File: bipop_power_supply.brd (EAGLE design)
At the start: 160 x 100 mm, 20 parts, among them IC1 LM1117MP-3.3, IC2 LM1117MP-5.0

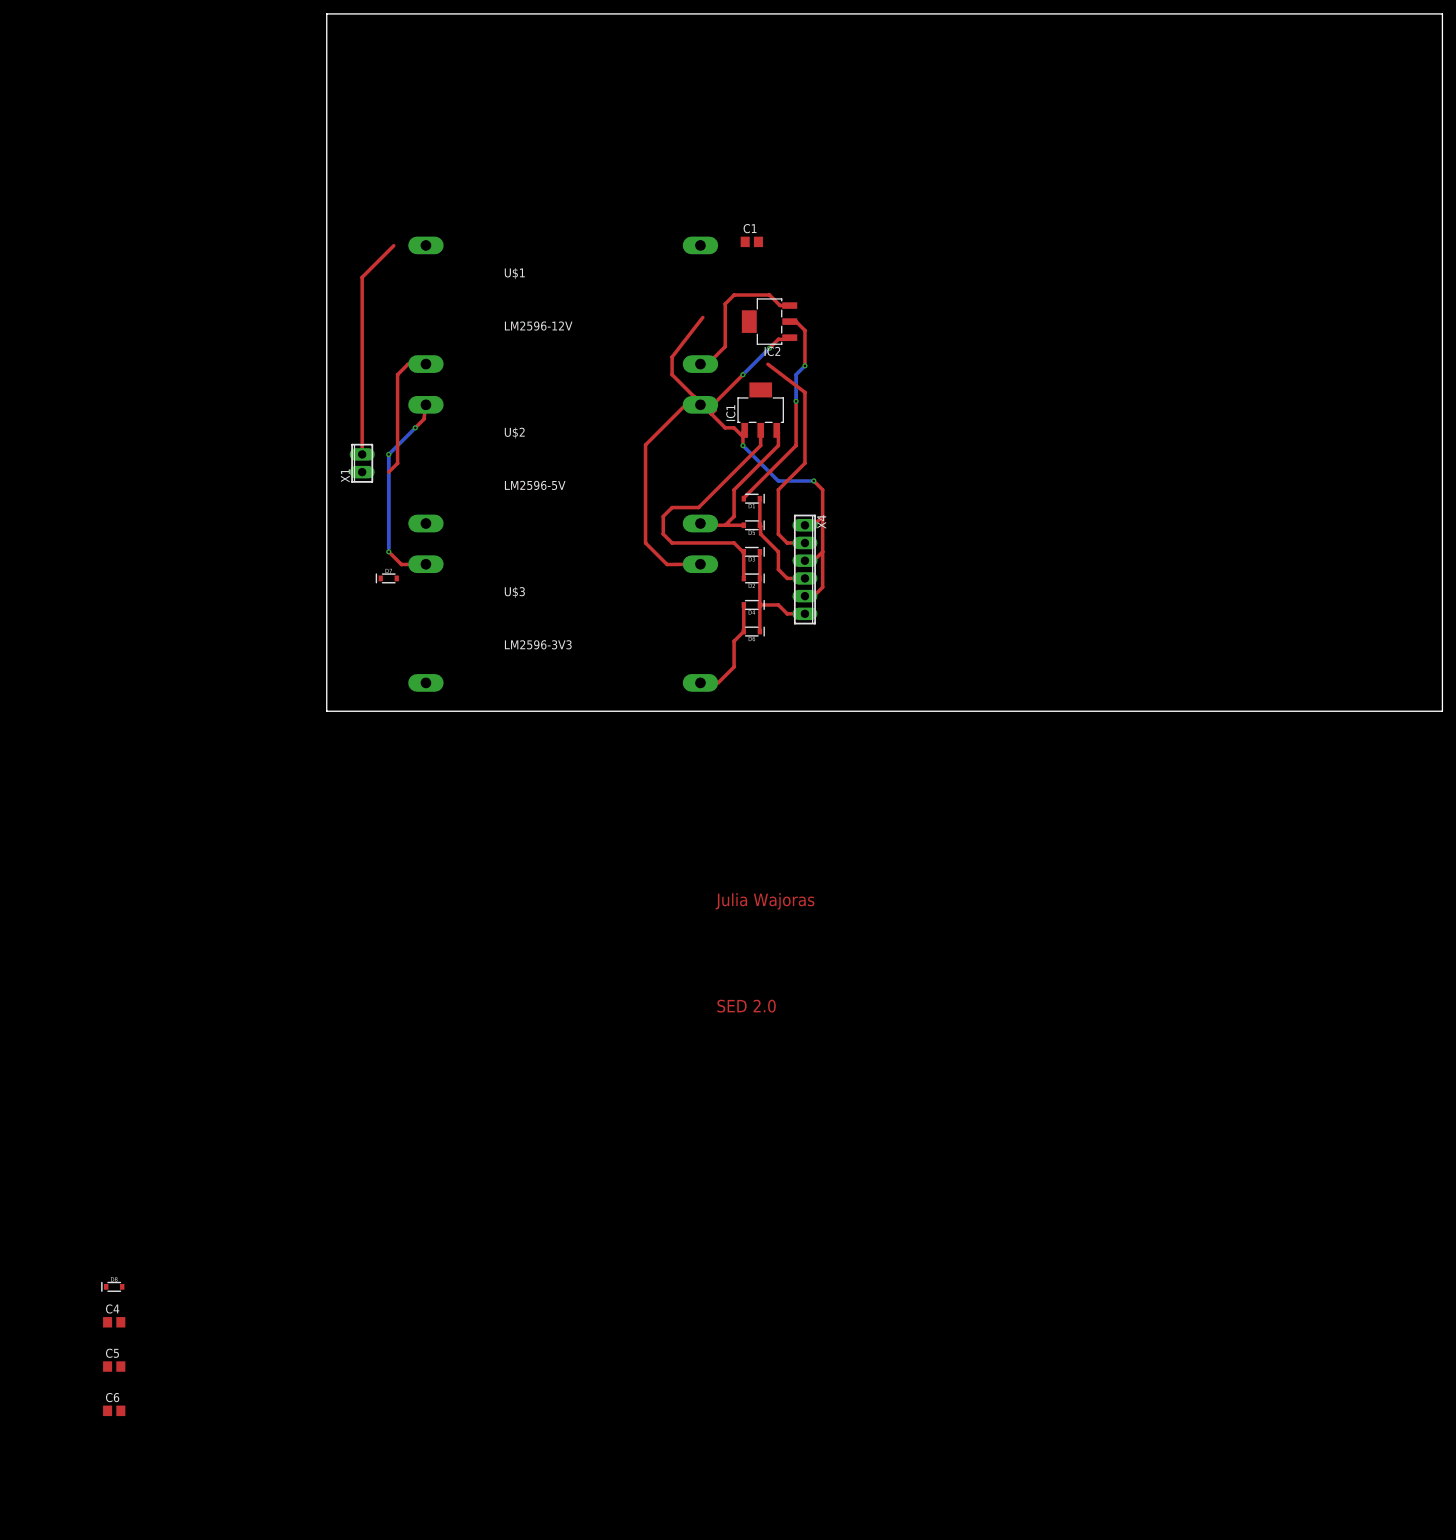
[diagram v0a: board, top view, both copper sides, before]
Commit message: .sch z diodami i kondensatorami, .brd TODO
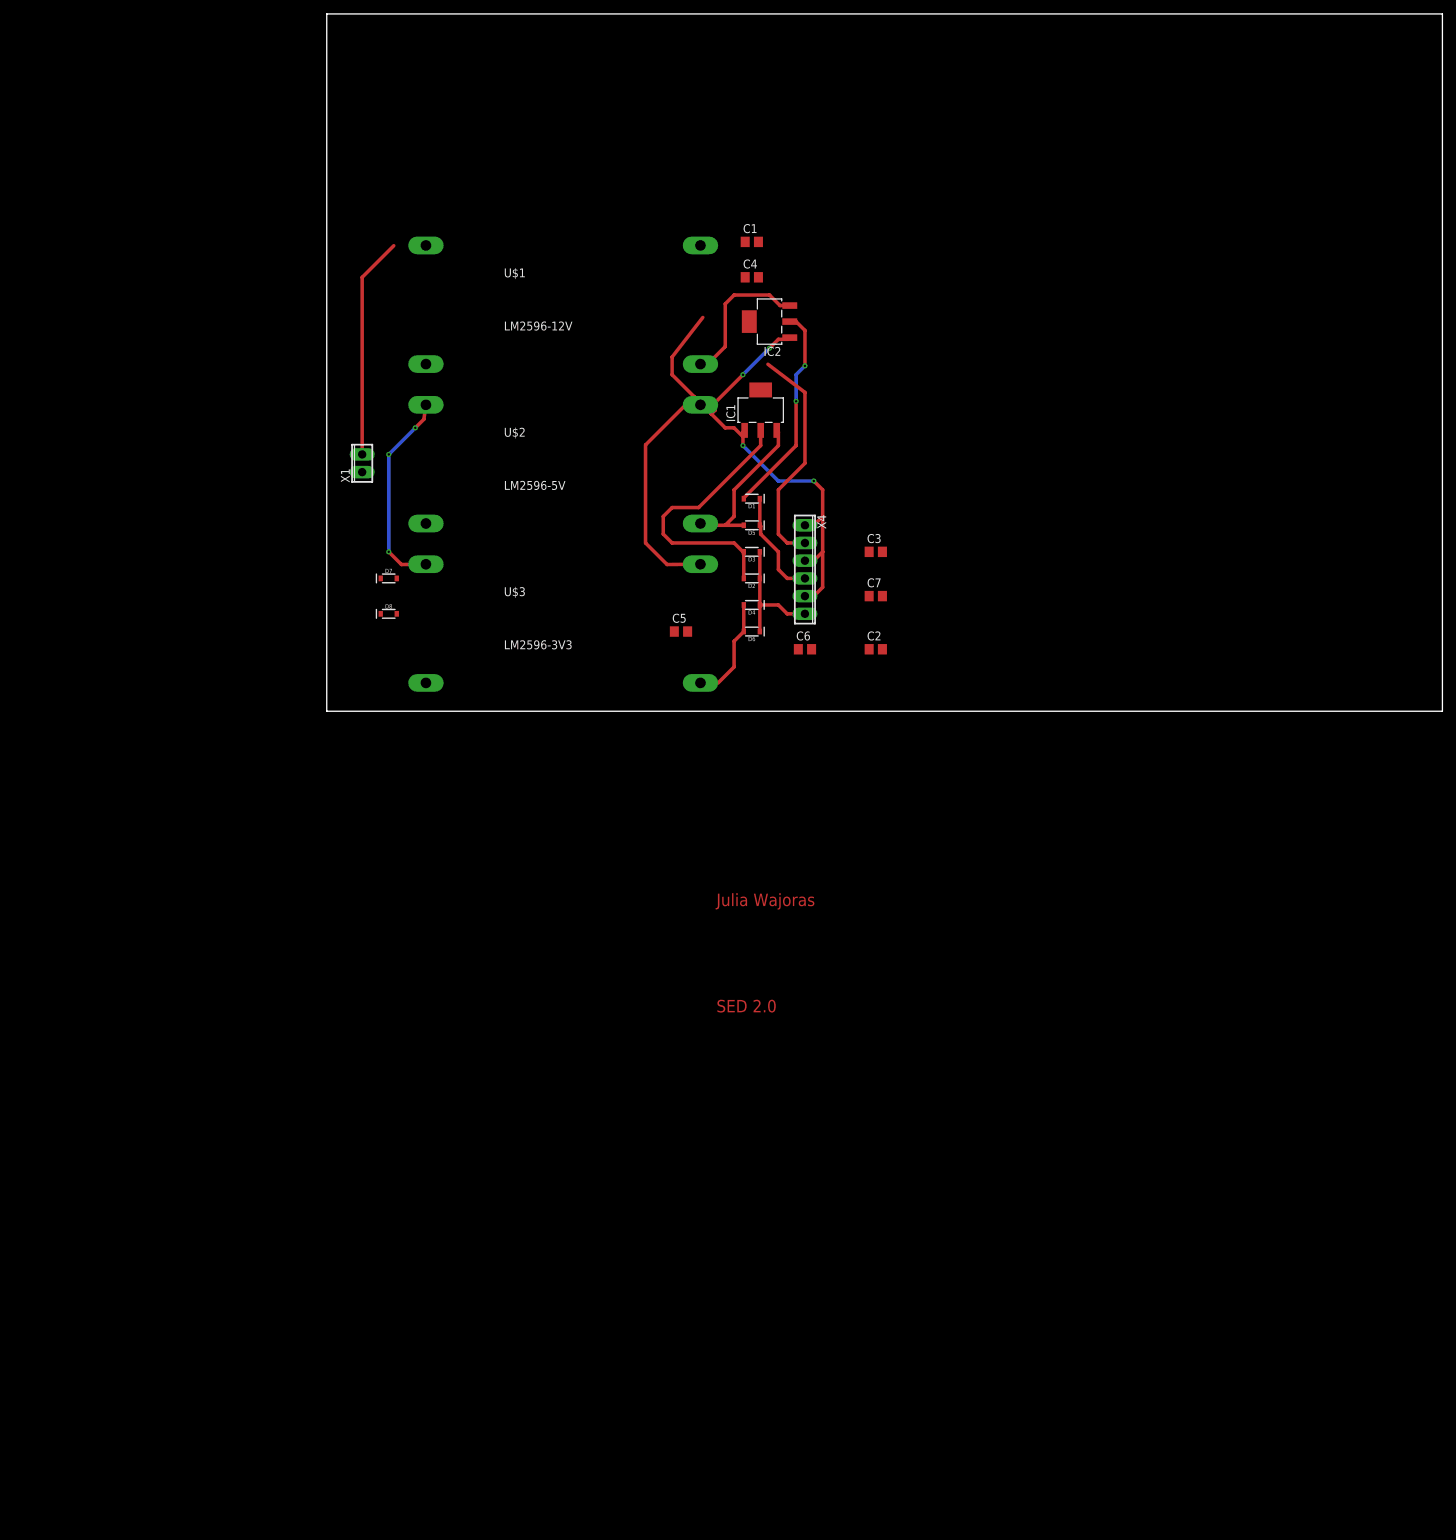
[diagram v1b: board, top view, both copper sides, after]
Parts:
- added C2, C3, C7: 100uF, rcl:C0805
- moved C4 175.6 mm to (61.0, 62.2)
- moved C6 147.5 mm to (68.6, 8.89)
- moved C5 133.1 mm to (50.8, 11.4)
- moved D8 104.2 mm to (8.89, 14.0)
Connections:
- removed net N$2: C1.2, C4.2, IC2.3, U$1.V_OUT+, X4.2
- removed net N$6: C1.1, C4.1, U$1.V_OUT-
- new net C12+: C7.1, IC2.3, U$1.V_OUT+, X4.2
- new net N$10: C1.1, C4.2
- new net N$12: C1.2, C3.1
- new net N$8: C2.2, C5.1
- new net N$9: C4.1, C7.2
- net GND: now also C2.1, C3.2, U$1.V_OUT-; no longer C5.1
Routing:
- net N$2: track 53.0 -> 0.00 mm
- net C12+: track 0.00 -> 53.0 mm
- net N$22: track 20.9 -> 1.75 mm
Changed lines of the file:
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@@
 </element>
 <element name="C1" library="rcl" library_urn="urn:adsk.eagle:library:334" package="C0805" package3d_urn="urn:adsk.eagle:package:23617/2" value="100uF" x="60.96" y="67.31"/>
-<element name="D8" library="SparkFun-DiscreteSemi" package="SOD-323" value="33.3V" x="-30.48" y="-82.55">
-<attribute name="PROD_ID" value="DIO-11284" x="-30.48" y="-82.55" size="1.778" layer="27" display="off"/>
+<element name="D8" library="SparkFun-DiscreteSemi" package="SOD-323" value="33.3V" x="8.89" y="13.97">
+<attribute name="PROD_ID" value="DIO-11284" x="8.89" y="13.97" size="1.778" layer="27" display="off"/>
 </element>
-<element name="C4" library="rcl" library_urn="urn:adsk.eagle:library:334" package="C0805" package3d_urn="urn:adsk.eagle:package:23617/2" value="100uF" x="-30.48" y="-87.63"/>
-<element name="C5" library="rcl" library_urn="urn:adsk.eagle:library:334" package="C0805" package3d_urn="urn:adsk.eagle:package:23617/2" value="100uF" x="-30.48" y="-93.98"/>
-<element name="C6" library="rcl" library_urn="urn:adsk.eagle:library:334" package="C0805" package3d_urn="urn:adsk.eagle:package:23617/2" value="100uF" x="-30.48" y="-100.33"/>
+<element name="C4" library="rcl" library_urn="urn:adsk.eagle:library:334" package="C0805" package3d_urn="urn:adsk.eagle:package:23617/2" value="100uF" x="60.96" y="62.23"/>
+<element name="C5" library="rcl" library_urn="urn:adsk.eagle:library:334" package="C0805" package3d_urn="urn:adsk.eagle:package:23617/2" value="100uF" x="50.8" y="11.43"/>
+<element name="C6" library="rcl" library_urn="urn:adsk.eagle:library:334" package="C0805" package3d_urn="urn:adsk.eagle:package:23617/2" value="100uF" x="68.58" y="8.89"/>
+<element name="C2" library="rcl" library_urn="urn:adsk.eagle:library:334" package="C0805" package3d_urn="urn:adsk.eagle:package:23617/2" value="100uF" x="78.74" y="8.89"/>
+<element name="C3" library="rcl" library_urn="urn:adsk.eagle:library:334" package="C0805" package3d_urn="urn:adsk.eagle:package:23617/2" value="100uF" x="78.74" y="22.86"/>
+<element name="C7" library="rcl" library_urn="urn:adsk.eagle:library:334" package="C0805" package3d_urn="urn:adsk.eagle:package:23617/2" value="100uF" x="78.74" y="16.51"/>
 </elements>
 <signals>
@@
 <wire x1="66.16" y1="53.34" x2="66.4" y2="53.58" width="0.508" layer="1"/>
 <contactref element="C6" pad="1"/>
-<contactref element="C5" pad="1"/>
+<contactref element="C2" pad="1"/>
 <contactref element="U$2" pad="V_OUT-"/>
-<wire x1="-31.43" y1="-93.98" x2="-31.43" y2="-100.33" width="0" layer="19" extent="1-1"/>
-<wire x1="48.81" y1="21.04" x2="-31.43" y2="-93.98" width="0" layer="19" extent="1-1"/>
+<contactref element="U$1" pad="V_OUT-"/>
+<contactref element="C3" pad="2"/>
+<wire x1="77.79" y1="8.89" x2="79.69" y2="22.86" width="0" layer="19" extent="1-1"/>
+<wire x1="67.63" y1="8.89" x2="77.79" y2="8.89" width="0" layer="19" extent="1-1"/>
+<wire x1="48.81" y1="21.04" x2="67.63" y2="8.89" width="0" layer="19" extent="1-1"/>
 <wire x1="53.93" y1="43.86" x2="53.89" y2="43.9" width="0" layer="19" extent="1-1"/>
 <wire x1="53.594" y1="43.942" x2="53.89" y2="43.9" width="0" layer="19" extent="1-1"/>
+<wire x1="53.594" y1="66.802" x2="53.93" y2="56.47" width="0" layer="19" extent="1-1"/>
 </signal>
 <signal name="N$5">
@@
 <contactref element="C6" pad="2"/>
 <contactref element="U$3" pad="V_OUT+"/>
-<wire x1="53.594" y1="4.064" x2="-29.53" y2="-100.33" width="0" layer="19" extent="1-1"/>
+<wire x1="53.594" y1="4.064" x2="69.53" y2="8.89" width="0" layer="19" extent="1-1"/>
 <wire x1="56.11" y1="4.04" x2="53.594" y2="4.064" width="0" layer="19" extent="1-1"/>
 </signal>
@@
 <wire x1="58.42" y1="31.75" x2="58.42" y2="27.94" width="0.508" layer="1"/>
 <contactref element="C5" pad="2"/>
-<wire x1="53.594" y1="26.924" x2="-29.53" y2="-93.98" width="0" layer="19" extent="1-1"/>
+<wire x1="53.594" y1="26.924" x2="51.75" y2="11.43" width="0" layer="19" extent="1-1"/>
 </signal>
 <signal name="N$11">
@@
 <wire x1="8.89" y1="36.83" x2="12.7" y2="40.64" width="0.508" layer="16"/>
 <wire x1="8.89" y1="22.86" x2="8.89" y2="36.83" width="0.508" layer="16"/>
+<contactref element="D7" pad="C"/>
 <contactref element="U$1" pad="V_IN-"/>
-<contactref element="D7" pad="C"/>
 <wire x1="14.224" y1="43.942" x2="14.224" y2="66.802" width="0" layer="19" extent="1-1"/>
 <wire x1="7.74" y1="19.05" x2="10.71" y2="21.04" width="0" layer="19" extent="1-1"/>
 </signal>
 <signal name="N$22">
-<contactref element="U$1" pad="V_IN+"/>
 <contactref element="U$2" pad="V_IN+"/>
 <wire x1="14.224" y1="26.924" x2="12.47" y2="26.9" width="0.508" layer="1"/>
-<wire x1="14.224" y1="49.784" x2="11.66" y2="49.76" width="0.508" layer="1"/>
-<wire x1="11.66" y1="49.76" x2="10.16" y2="48.26" width="0.508" layer="1"/>
-<wire x1="10.16" y1="35.56" x2="8.89" y2="34.29" width="0.508" layer="1"/>
-<wire x1="10.16" y1="48.26" x2="10.16" y2="35.56" width="0.508" layer="1"/>
 <contactref element="U$3" pad="V_IN+"/>
 <contactref element="X1" pad="1"/>
 <contactref element="D8" pad="A"/>
-<wire x1="14.224" y1="4.064" x2="-29.33" y2="-82.55" width="0" layer="19" extent="1-1"/>
+<contactref element="U$1" pad="V_IN+"/>
+<wire x1="14.224" y1="4.064" x2="10.04" y2="13.97" width="0" layer="19" extent="1-1"/>
 <wire x1="14.224" y1="26.924" x2="14.224" y2="4.064" width="0" layer="19" extent="1-1"/>
-<wire x1="8.89" y1="34.29" x2="12.47" y2="26.9" width="0" layer="19" extent="1-1"/>
-<wire x1="5.08" y1="34.29" x2="8.89" y2="34.29" width="0" layer="19" extent="1-1"/>
-</signal>
-<signal name="N$2">
+<wire x1="5.08" y1="34.29" x2="12.47" y2="26.9" width="0" layer="19" extent="1-1"/>
+<wire x1="14.224" y1="49.784" x2="5.08" y2="34.29" width="0" layer="19" extent="1-1"/>
+</signal>
+<signal name="N$1">
+<contactref element="X1" pad="2"/>
+<contactref element="D7" pad="A"/>
+<wire x1="9.61" y1="66.76" x2="5.08" y2="62.23" width="0.508" layer="1"/>
+<wire x1="5.08" y1="62.23" x2="5.08" y2="36.83" width="0.508" layer="1"/>
+<contactref element="D8" pad="C"/>
+<wire x1="10.04" y1="19.05" x2="7.74" y2="13.97" width="0" layer="19" extent="1-1"/>
+<wire x1="5.08" y1="36.83" x2="10.04" y2="19.05" width="0" layer="19" extent="1-1"/>
+</signal>
+<signal name="N$8">
+<contactref element="C5" pad="1"/>
+<contactref element="C2" pad="2"/>
+<wire x1="49.85" y1="11.43" x2="79.69" y2="8.89" width="0" layer="19" extent="1-1"/>
+</signal>
+<signal name="C12+">
+<contactref element="C7" pad="1"/>
 <contactref element="X4" pad="2"/>
 <contactref element="IC2" pad="3"/>
@@
 <wire x1="57.15" y1="52.3" x2="57.15" y2="58.42" width="0.508" layer="1"/>
 <wire x1="54.61" y1="49.76" x2="57.15" y2="52.3" width="0.508" layer="1"/>
+<contactref element="U$1" pad="V_OUT+"/>
+<wire x1="66.04" y1="24.13" x2="77.79" y2="16.51" width="0" layer="19" extent="1-1"/>
+<wire x1="57.15" y1="52.3" x2="63.27" y2="49.76" width="0" layer="19" extent="1-1"/>
+<wire x1="53.594" y1="49.784" x2="54.61" y2="49.76" width="0" layer="19" extent="1-1"/>
+</signal>
+<signal name="N$9">
+<contactref element="C7" pad="2"/>
+<contactref element="C4" pad="1"/>
+<wire x1="60.01" y1="62.23" x2="79.69" y2="16.51" width="0" layer="19" extent="1-1"/>
+</signal>
+<signal name="N$10">
+<contactref element="C4" pad="2"/>
+<contactref element="C1" pad="1"/>
+<wire x1="60.01" y1="67.31" x2="61.91" y2="62.23" width="0" layer="19" extent="1-1"/>
+</signal>
+<signal name="N$12">
 <contactref element="C1" pad="2"/>
-<contactref element="C4" pad="2"/>
-<contactref element="U$1" pad="V_OUT+"/>
-<wire x1="63.5" y1="59.69" x2="61.91" y2="67.31" width="0" layer="19" extent="1-1"/>
-<wire x1="53.594" y1="49.784" x2="54.61" y2="49.76" width="0" layer="19" extent="1-1"/>
-<wire x1="63.27" y1="49.76" x2="57.15" y2="52.3" width="0" layer="19" extent="1-1"/>
-<wire x1="-29.53" y1="-87.63" x2="66.04" y2="24.13" width="0" layer="19" extent="1-1"/>
-</signal>
-<signal name="N$1">
-<contactref element="X1" pad="2"/>
-<contactref element="D7" pad="A"/>
-<wire x1="9.61" y1="66.76" x2="5.08" y2="62.23" width="0.508" layer="1"/>
-<wire x1="5.08" y1="62.23" x2="5.08" y2="36.83" width="0.508" layer="1"/>
-<contactref element="D8" pad="C"/>
-<wire x1="10.04" y1="19.05" x2="-31.63" y2="-82.55" width="0" layer="19" extent="1-1"/>
-<wire x1="5.08" y1="36.83" x2="10.04" y2="19.05" width="0" layer="19" extent="1-1"/>
-</signal>
-<signal name="N$6">
-<contactref element="C1" pad="1"/>
-<contactref element="U$1" pad="V_OUT-"/>
-<contactref element="C4" pad="1"/>
-<wire x1="53.594" y1="66.802" x2="60.01" y2="67.31" width="0" layer="19" extent="1-1"/>
-<wire x1="-31.43" y1="-87.63" x2="53.594" y2="66.802" width="0" layer="19" extent="1-1"/>
+<contactref element="C3" pad="1"/>
+<wire x1="61.91" y1="67.31" x2="77.79" y2="22.86" width="0" layer="19" extent="1-1"/>
 </signal>
 </signals>
